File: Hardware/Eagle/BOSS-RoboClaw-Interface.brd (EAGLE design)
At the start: 41.4 x 48.3 mm, 10 parts, among them IC1 ISO7221AQDRQ1, J1 MOLEX 22112024, J2 MOLEX 22122034, J3 Amphenol 75869-130LF, J5 SAMTEC ESQ-110-33-T-D, J6 SAMTEC-ESQ-105-33-T-S, X1 Amphenol L77SDAH15SOL2RM8C309

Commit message: Changed limit switch pullup to 4.7K
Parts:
- R1: value 10K -> 4K7
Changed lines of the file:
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@@
 <attribute name="NAME" x="5.7785" y="8.255" size="1.016" layer="26" rot="MR180"/>
 </element>
-<element name="R1" library="AUmlib" library_urn="urn:adsk.eagle:library:9166017" package="R0805" package3d_urn="urn:adsk.eagle:package:4021199/4" value="10K" x="33.02" y="25.0825" smashed="yes" rot="R270">
+<element name="R1" library="AUmlib" library_urn="urn:adsk.eagle:library:9166017" package="R0805" package3d_urn="urn:adsk.eagle:package:4021199/4" value="4K7" x="33.02" y="25.0825" smashed="yes" rot="R270">
 <attribute name="NAME" x="35.8775" y="25.7175" size="1.016" layer="25" font="vector" rot="R180"/>
 <attribute name="SPICEPREFIX" value="R" x="33.02" y="25.0825" size="1.778" layer="27" rot="R270" display="off"/>

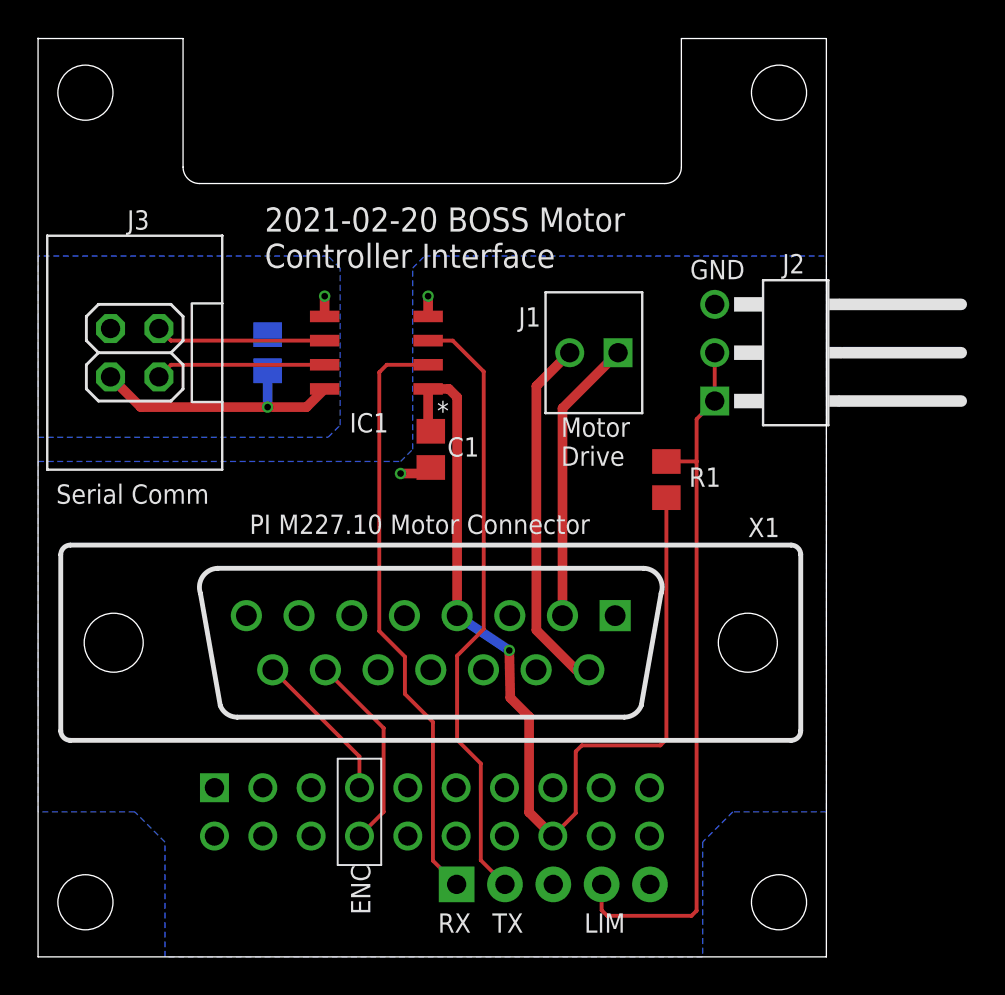
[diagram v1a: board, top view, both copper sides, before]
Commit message: Created a motor breakout board
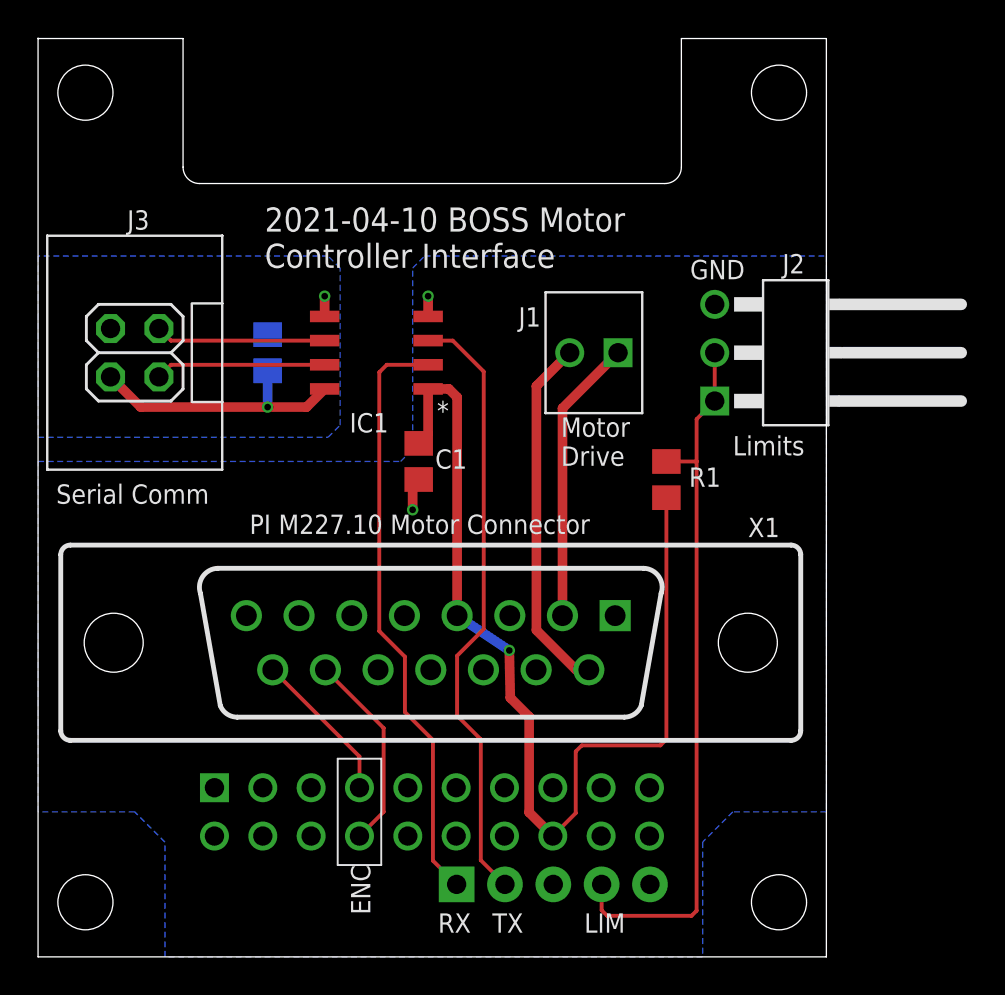
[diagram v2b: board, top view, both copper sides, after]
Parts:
- moved C1 0.90 mm to (20.0, 26.0)
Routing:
- net VCC1: track 52.1 -> 52.9 mm
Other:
- board text added: "2021-04-10 BOSS Motor Controller Interface"
- board text added: "Limits"
- board text removed: "2021-02-20 BOSS Motor Controller Interface"
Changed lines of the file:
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@@
 <board>
 <description>Basic Micro 2x7A RoboClaw interface to PI M-227.10 motor mikel.</description>
-<fusionsync huburn="a.cGVyc29uYWw6dWUyZDgyNjcx" projecturn="a.cGVyc29uYWw6dWUyZDgyNjcxIzIwMTgxMjIwMTY2NDc1MjMx" f3durn="urn:adsk.wipprod:dm.lineage:qemoZLx4Q2igI8rCdvDi4A" pcbguid="dc5b1513-d717-4bee-81ed-ee262294f200" lastpulledtime="" lastsyncedchangeguid="640551e2-8e01-6089-9af3-421ee07b5960" latestrevisionid="" lastsyncedrevisionid="" lastboardhashguid="5ea78dc1-fa9a-b686-c250-1ae1f5f38843" lastpushedtime="2020-11-23T17:20:39Z" linktopcb3d="false"/>
+<fusionsync huburn="a.cGVyc29uYWw6dWUyZDgyNjcx" projecturn="a.cGVyc29uYWw6dWUyZDgyNjcxIzIwMTgxMjIwMTY2NDc1MjMx" f3durn="urn:adsk.wipprod:dm.lineage:qemoZLx4Q2igI8rCdvDi4A" pcbguid="dc5b1513-d717-4bee-81ed-ee262294f200" lastpulledtime="" lastsyncedchangeguid="640551e2-8e01-6089-9af3-421ee07b5960" latestrevisionid="" lastsyncedrevisionid="" lastboardhashguid="2dc59ba5-d706-44c4-1f31-abdfe371d1e9" lastpushedtime="2021-04-08T02:20:39Z" linktopcb3d="false"/>
 <plain>
 <wire x1="0" y1="0" x2="41.4274" y2="0" width="0" layer="20"/>
@@
 <wire x1="8.4836" y1="40.64" x2="32.9438" y2="40.64" width="0" layer="20"/>
 <wire x1="33.8074" y1="48.26" x2="41.4274" y2="48.26" width="0" layer="20"/>
-<text x="11.9126" y="36.2077" size="1.27" layer="21" font="vector">2021-02-20 BOSS Motor
+<text x="11.9126" y="36.2077" size="1.27" layer="21" font="vector">2021-04-10 BOSS Motor
 Controller Interface</text>
 <text x="34.2646" y="35.6108" size="1.016" layer="21" font="vector">GND</text>
@@
 <text x="9.2075" y="32.385" size="1.016" layer="22" rot="MR0">TX</text>
 <text x="9.2075" y="29.845" size="1.016" layer="22" rot="MR0">RX</text>
-<text x="4.7625" y="28.2575" size="1.016" layer="22" rot="MR0">+5V</text>
+<text x="5.08" y="27.94" size="1.016" layer="22" rot="MR0">+5V</text>
 <text x="5.08" y="34.29" size="1.016" layer="22" rot="MR0">GND
 -ISO</text>
+<text x="36.5125" y="26.3525" size="1.016" layer="21">Limits</text>
 </plain>
 <attributes>
@@
 <attribute name="OC_NEWARK" value="unknown" x="53.6575" y="10.16" size="1.778" layer="27" display="off"/>
 </element>
-<element name="C1" library="AUmlib" library_urn="urn:adsk.eagle:library:9166017" package="C0805" package3d_urn="urn:adsk.eagle:package:4021265/3" value="0.1uF" x="20.6375" y="26.67" smashed="yes" rot="R270">
-<attribute name="NAME" x="23.1775" y="27.305" size="1.016" layer="25" font="vector" rot="R180"/>
-<attribute name="SPICEPREFIX" value="C" x="20.6375" y="26.67" size="1.778" layer="27" rot="R270" display="off"/>
+<element name="C1" library="AUmlib" library_urn="urn:adsk.eagle:library:9166017" package="C0805" package3d_urn="urn:adsk.eagle:package:4021265/3" value="0.1uF" x="20.0025" y="26.035" smashed="yes" rot="R270">
+<attribute name="NAME" x="22.5425" y="26.67" size="1.016" layer="25" font="vector" rot="R180"/>
+<attribute name="SPICEPREFIX" value="C" x="20.0025" y="26.035" size="1.778" layer="27" rot="R270" display="off"/>
 </element>
 <element name="C2" library="AUmlib" library_urn="urn:adsk.eagle:library:9166017" package="C0805" package3d_urn="urn:adsk.eagle:package:4021265/3" value="0.1uF" x="12.065" y="31.75" smashed="yes" rot="MR90">
@@
 </element>
 <element name="J6" library="AUmlib" library_urn="urn:adsk.eagle:library:9166017" package="1X05-ESQ-105-33-T-S" package3d_urn="urn:adsk.eagle:package:24929591/4" value="SAMTEC-ESQ-105-33-T-S" x="27.0764" y="3.81" smashed="yes" rot="MR180">
-<attribute name="NAME" x="18.5039" y="4.0005" size="1.016" layer="26" font="vector" rot="MR180"/>
+<attribute name="NAME" x="18.8214" y="3.683" size="1.016" layer="26" font="vector" rot="MR180"/>
 </element>
 <element name="J5" library="AUmlib" library_urn="urn:adsk.eagle:library:9166017" package="2X10-ESQ-110-33-T-D" package3d_urn="urn:adsk.eagle:package:24929474/2" value="SAMTEC ESQ-110-33-T-D" x="20.701" y="7.62" smashed="yes" rot="MR180">
-<attribute name="NAME" x="5.7785" y="8.255" size="1.016" layer="26" rot="MR180"/>
+<attribute name="NAME" x="6.096" y="6.35" size="1.016" layer="26" rot="MR180"/>
 </element>
 <element name="R1" library="AUmlib" library_urn="urn:adsk.eagle:library:9166017" package="R0805" package3d_urn="urn:adsk.eagle:package:4021199/4" value="4K7" x="33.02" y="25.0825" smashed="yes" rot="R270">
@@
 <contactref element="X1" pad="6"/>
 <contactref element="J5" pad="15"/>
-<wire x1="20.6375" y1="25.72" x2="20.3175" y2="25.4" width="0.508" layer="1"/>
-<wire x1="20.3175" y1="25.4" x2="19.05" y2="25.4" width="0.508" layer="1"/>
-<via x="19.05" y="25.4" extent="1-16" drill="0.35"/>
+<wire x1="20.0025" y1="25.085" x2="19.685" y2="24.7675" width="0.508" layer="1"/>
+<wire x1="19.685" y1="24.7675" x2="19.685" y2="23.495" width="0.508" layer="1"/>
+<via x="19.685" y="23.495" extent="1-16" drill="0.35"/>
 </signal>
 <signal name="ROBO-RX">
 <contactref element="IC1" pad="2"/>
-<wire x1="20.7518" y1="12.3444" x2="19.2786" y2="13.8176" width="0.2032" layer="1"/>
+<wire x1="20.7518" y1="11.3919" x2="19.2786" y2="12.8651" width="0.2032" layer="1"/>
 <wire x1="18.3261" y1="31.115" x2="20.4978" y2="31.115" width="0.2032" layer="1"/>
-<wire x1="20.7518" y1="5.0546" x2="20.7518" y2="12.3444" width="0.2032" layer="1"/>
-<wire x1="19.2786" y1="13.8176" x2="19.2786" y2="15.7734" width="0.2032" layer="1"/>
+<wire x1="20.7518" y1="5.0546" x2="20.7518" y2="11.3919" width="0.2032" layer="1"/>
+<wire x1="19.2786" y1="12.8651" x2="19.2786" y2="15.7734" width="0.2032" layer="1"/>
 <wire x1="19.2786" y1="15.7734" x2="17.9324" y2="17.1196" width="0.2032" layer="1"/>
 <wire x1="17.9324" y1="17.1196" x2="17.9324" y2="30.7213" width="0.2032" layer="1"/>
@@
 <wire x1="23.4188" y1="30.7594" x2="23.4188" y2="17.2212" width="0.2032" layer="1"/>
 <wire x1="23.4188" y1="17.2212" x2="22.0218" y2="15.8242" width="0.2032" layer="1"/>
-<wire x1="22.0218" y1="15.8242" x2="22.0218" y2="11.4046" width="0.2032" layer="1"/>
-<wire x1="23.2664" y1="10.16" x2="22.0218" y2="11.4046" width="0.2032" layer="1"/>
+<wire x1="22.0218" y1="15.8242" x2="22.0218" y2="12.6746" width="0.2032" layer="1"/>
+<wire x1="23.2664" y1="11.43" x2="22.0218" y2="12.6746" width="0.2032" layer="1"/>
 <contactref element="J6" pad="2"/>
 <wire x1="24.5364" y1="3.81" x2="23.2664" y2="5.08" width="0.2032" layer="1"/>
-<wire x1="23.2664" y1="5.08" x2="23.2664" y2="10.16" width="0.2032" layer="1"/>
+<wire x1="23.2664" y1="5.08" x2="23.2664" y2="11.43" width="0.2032" layer="1"/>
 </signal>
 <signal name="LIMIT">
@@
 <wire x1="21.59" y1="29.845" x2="20.4978" y2="29.845" width="0.508" layer="1"/>
 <wire x1="22.0218" y1="29.4132" x2="21.59" y2="29.845" width="0.508" layer="1"/>
-<wire x1="20.4978" y1="29.845" x2="20.4978" y2="27.7597" width="0.508" layer="1"/>
-<wire x1="20.4978" y1="27.7597" x2="20.6375" y2="27.62" width="0.508" layer="1"/>
+<wire x1="20.4978" y1="29.845" x2="20.4978" y2="27.4803" width="0.508" layer="1"/>
+<wire x1="20.4978" y1="27.4803" x2="20.0025" y2="26.985" width="0.508" layer="1"/>
 <wire x1="27.051" y1="6.35" x2="28.2575" y2="7.5565" width="0.2032" layer="1"/>
 <wire x1="28.2575" y1="10.795" x2="28.575" y2="11.1125" width="0.2032" layer="1"/>

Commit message: Includes open drain buffer
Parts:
- added C3: 0.1uF, AUmlib:C0805
- added U1: MC74VHC1G07DTT1G, AUmlib:SOT23-5_ONS-M
- J1: value MOLEX 22112024 -> MOLEX 22112022
- moved C2 6.11 mm to (18.1, 30.8)
- moved C1 3.81 mm to (23.8, 26.0)
- moved IC1 3.17 mm to (21.0, 31.8)
- moved J1 1.59 mm to (30.8, 31.8)
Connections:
- net ROBO0TX renamed ROBO-TX
- removed net TX: IC1.6, J3.3
- new net TX-ISO: IC1.6, U1.2
- new net TX-PULLUP: J3.3, U1.4
- net GND-ISO: now also C3.2, U1.3
- net VCC2: now also C3.1, U1.5
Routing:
- net VCC2: track 14.2 -> 25.5 mm, vias 1 -> 3
- net TX: track 8.98 -> 0.00 mm
- net TX-PULLUP: track 0.00 -> 6.42 mm
- net TX-ISO: track 0.00 -> 3.89 mm
- net RX: track 8.98 -> 12.2 mm
- net GND-ISO: track 1.07 -> 2.92 mm, vias 1 -> 2
- net ROBO-RX: track 31.3 -> 32.1 mm
- net M1B: track 18.9 -> 19.6 mm
- net M1A: track 15.0 -> 15.7 mm
- net GND: track 2.79 -> 3.29 mm
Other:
- board text added: "2022-02-28 BOSS Motor Controller Interface"
- board text removed: "2021-04-10 BOSS Motor Controller Interface"
